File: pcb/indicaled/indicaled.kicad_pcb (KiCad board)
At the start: 2 copper layers, 17 parts

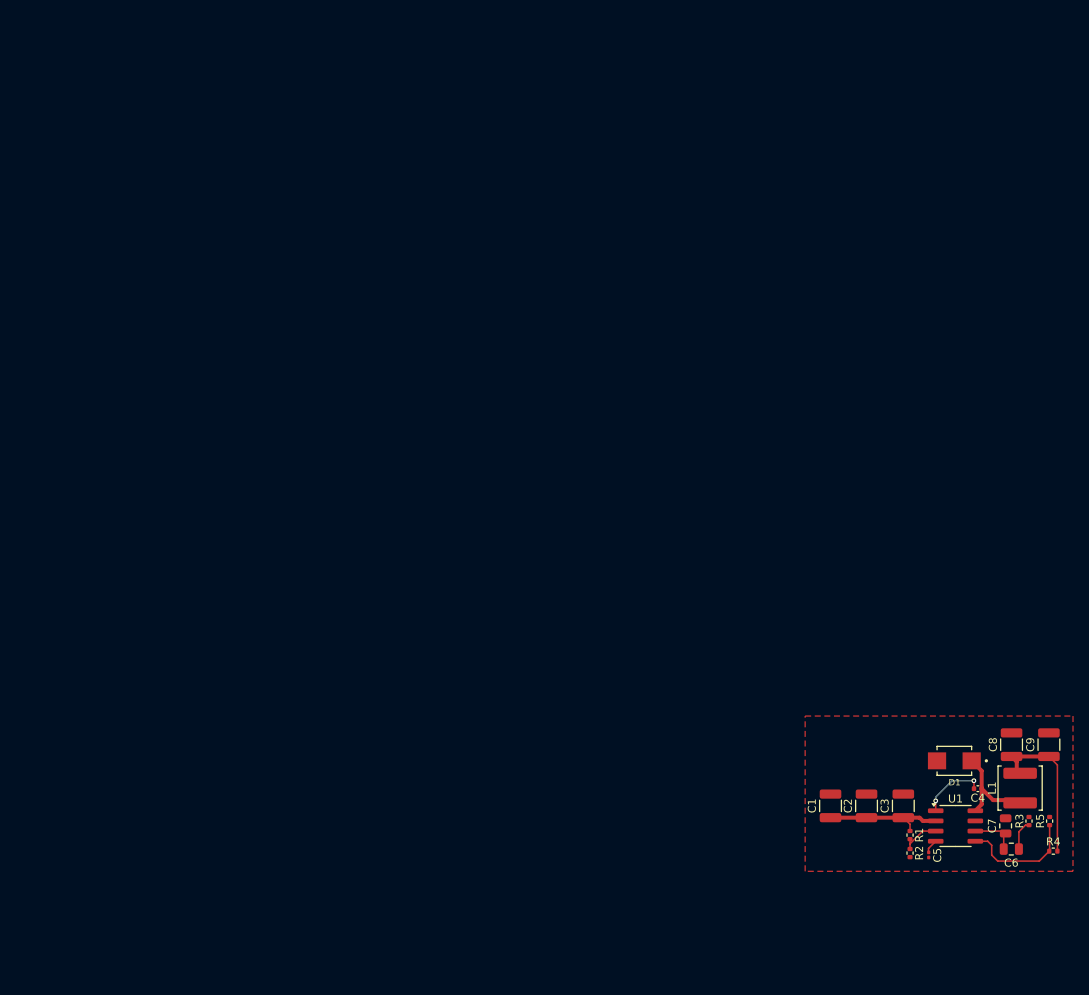
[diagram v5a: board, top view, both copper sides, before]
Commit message: adicionando os transistores que vão retificar o sinal do caro pro ESP
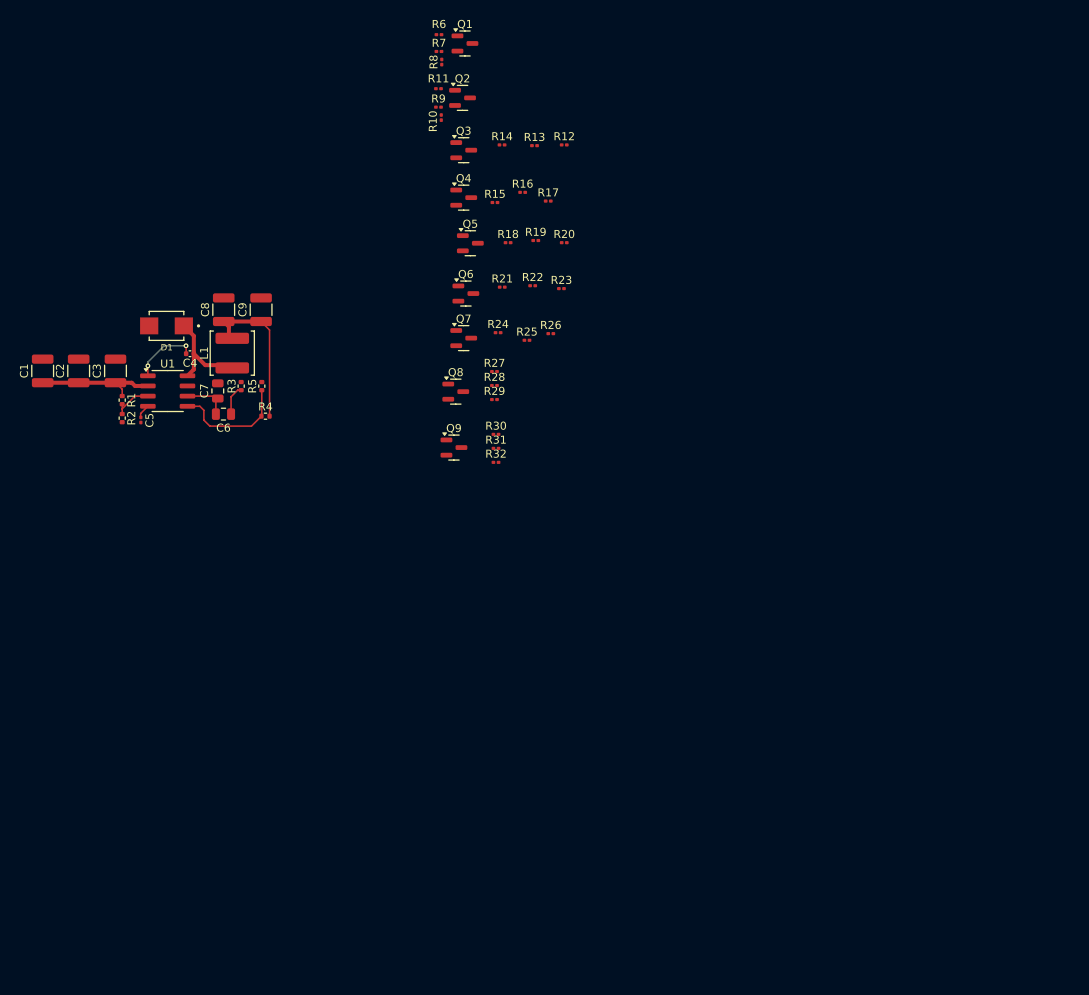
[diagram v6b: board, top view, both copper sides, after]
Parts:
- added Q1: NPN, Package_TO_SOT_SMD:SOT-23, F.Cu at (130.0, 26.2)
- added Q2: NPN, Package_TO_SOT_SMD:SOT-23, F.Cu at (129.7, 33.0)
- added Q3: NPN, Package_TO_SOT_SMD:SOT-23, F.Cu at (129.8, 39.5)
- added Q4: NPN, Package_TO_SOT_SMD:SOT-23, F.Cu at (129.8, 45.5)
- added Q5: NPN, Package_TO_SOT_SMD:SOT-23, F.Cu at (130.7, 51.2)
- added Q6: NPN, Package_TO_SOT_SMD:SOT-23, F.Cu at (130.1, 57.5)
- added Q7: NPN, Package_TO_SOT_SMD:SOT-23, F.Cu at (129.8, 63.0)
- added Q8: NPN, Package_TO_SOT_SMD:SOT-23, F.Cu at (128.9, 69.7)
- added Q9: NPN, Package_TO_SOT_SMD:SOT-23, F.Cu at (128.6, 76.7)
- added R10: 2k, Resistor_SMD:R_0201_0603Metric, F.Cu at (127.0, 35.5)
- added R11: 1k, Resistor_SMD:R_0201_0603Metric, F.Cu at (126.7, 31.9)
- added R12: 10k, Resistor_SMD:R_0201_0603Metric, F.Cu at (142.4, 38.9)
- added R13: 2k, Resistor_SMD:R_0201_0603Metric, F.Cu at (138.7, 39.0)
- added R14: 1k, Resistor_SMD:R_0201_0603Metric, F.Cu at (134.6, 38.9)
- added R15: 10k, Resistor_SMD:R_0201_0603Metric, F.Cu at (133.8, 46.1)
- added R16: 2k, Resistor_SMD:R_0201_0603Metric, F.Cu at (137.2, 44.8)
- added R17: 1k, Resistor_SMD:R_0201_0603Metric, F.Cu at (140.4, 45.9)
- added R18: 10k, Resistor_SMD:R_0201_0603Metric, F.Cu at (135.4, 51.1)
- added R19: 2k, Resistor_SMD:R_0201_0603Metric, F.Cu at (138.9, 50.8)
- added R20: 1k, Resistor_SMD:R_0201_0603Metric, F.Cu at (142.4, 51.1)
- added R21: 10k, Resistor_SMD:R_0201_0603Metric, F.Cu at (134.7, 56.7)
- added R22: 2k, Resistor_SMD:R_0201_0603Metric, F.Cu at (138.5, 56.5)
- added R23: 1k, Resistor_SMD:R_0201_0603Metric, F.Cu at (142.1, 56.8)
- added R24: 10k, Resistor_SMD:R_0201_0603Metric, F.Cu at (134.1, 62.4)
- added R25: 2k, Resistor_SMD:R_0201_0603Metric, F.Cu at (137.8, 63.3)
- added R26: 1k, Resistor_SMD:R_0201_0603Metric, F.Cu at (140.7, 62.5)
- added R27: 10k, Resistor_SMD:R_0201_0603Metric, F.Cu at (133.7, 67.2)
- added R28: 2k, Resistor_SMD:R_0201_0603Metric, F.Cu at (133.7, 69.0)
- added R29: 1k, Resistor_SMD:R_0201_0603Metric, F.Cu at (133.7, 70.7)
- added R30: 10k, Resistor_SMD:R_0201_0603Metric, F.Cu at (133.9, 75.1)
- added R31: 2k, Resistor_SMD:R_0201_0603Metric, F.Cu at (133.9, 76.8)
- added R32: 1k, Resistor_SMD:R_0201_0603Metric, F.Cu at (133.9, 78.6)
- added R6: 1k, Resistor_SMD:R_0201_0603Metric, F.Cu at (126.8, 25.1)
- added R7: 10k, Resistor_SMD:R_0201_0603Metric, F.Cu at (126.8, 27.2)
- added R8: 2k, Resistor_SMD:R_0201_0603Metric, F.Cu at (127.1, 28.5)
- added R9: 10k, Resistor_SMD:R_0201_0603Metric, F.Cu at (126.7, 34.2)
- moved C3 112.5 mm to (86.3, 67.1)
- moved C6 112.5 mm to (99.8, 72.5)
- moved C8 112.5 mm to (99.8, 59.5)
- moved R4 112.5 mm to (105.1, 72.8)
- moved C4 112.5 mm to (95.6, 65.0)
- moved C7 112.5 mm to (99.1, 69.6)
- moved C9 112.5 mm to (104.5, 59.5)
- moved D1 112.5 mm to (92.7, 61.5)
- moved L1 112.5 mm to (100.9, 64.9)
- moved R5 112.5 mm to (104.6, 69.0)
- moved C1 112.5 mm to (77.2, 67.1)
- moved C2 112.5 mm to (81.7, 67.1)
- moved C5 112.5 mm to (89.5, 73.3)
- moved R1 112.5 mm to (87.2, 70.8)
- moved R2 112.5 mm to (87.2, 73.0)
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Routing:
- removed copper zone on F.Cu, net GND
